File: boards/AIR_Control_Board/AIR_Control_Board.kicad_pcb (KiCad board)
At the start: 2 copper layers, 0 parts

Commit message: adding AIR folder
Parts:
- added C1: CP_1mF, footprints:C_Radial_D10_L13_P5_OEM, F.Cu at (231.1, 62.2)
- added C10: C_0.1uF, footprints:C_0805_OEM, F.Cu at (194.3, 67.3)
- added C2: C_0.1uF, footprints:C_0805_OEM, F.Cu at (191.8, 67.3)
- added C3: CP_1mF, footprints:C_Radial_D10_L13_P5_OEM, F.Cu at (217.2, 64.8)
- added C4: C_100pF, footprints:C_0805_OEM, F.Cu at (212.1, 52.1)
- added C5: C_22uF, footprints:C_1206_OEM, F.Cu at (210.6, 42.9)
- added C6: C_0.1uF, footprints:C_0805_OEM, F.Cu at (214.6, 38.1)
- added C7: C_30pF, footprints:C_0805_OEM, F.Cu at (207.0, 66.0)
- added C8: C_30pF, footprints:C_0805_OEM, F.Cu at (210.8, 67.3)
- added C9: C_47uF, footprints:C_0805_OEM, F.Cu at (221.0, 47.0)
- added D1: D_Schottky_SOD123, footprints:D_SOD-123W_OEM, F.Cu at (231.1, 52.1)
- added D10: LED_0805, footprints:LED_0805_OEM, F.Cu at (199.4, 48.3)
- added D11: D_Zener_18V, footprints:DO-214AA, F.Cu at (196.8, 39.4)
- added D2: D_Schottky_SOD123, footprints:D_SOD-123W_OEM, F.Cu at (232.4, 67.3)
- added D3: LED_0805, footprints:LED_0805_OEM, F.Cu at (198.8, 73.0)
- added D4: LED_0805, footprints:LED_0805_OEM, F.Cu at (210.2, 73.0)
- added D5: LED_0805, footprints:LED_0805_OEM, F.Cu at (222.9, 73.0)
- added D6: D_Schottky_SOD123, footprints:D_SOD-123W_OEM, F.Cu at (231.8, 40.0)
- added D7: LED_0805, footprints:LED_0805_OEM, F.Cu at (210.3, 38.4)
- added D8: LED_0805, footprints:LED_0805_OEM, F.Cu at (217.2, 52.1)
- added D9: LED_0805, footprints:LED_0805_OEM, F.Cu at (195.6, 48.3)
- added F1: F_500mA_16V, footprints:Fuse_1210, F.Cu at (203.2, 39.4)
- added IC1: ATMEGA16M1, footprints:TQFP-32_7x7mm_Pitch0.8mm, F.Cu at (204.5, 55.9)
- added J1: micromatch_female_RA_16, footprints:micromatch_female_ra_16, F.Cu at (189.2, 44.5)
- added J2: Ultrafit_2, footprints:Ultrafit_2, F.Cu at (243.8, 57.1)
- added J3: Ultrafit_2, footprints:Ultrafit_2, F.Cu at (243.8, 47.0)
- added J4: Ultrafit_2, footprints:Ultrafit_2, F.Cu at (243.8, 68.6)
- added J5: CONN_02X03, footprints:Pin_Header_Straight_2x03, F.Cu at (191.8, 77.5)
- added L1: L_4.7uH, footprints:4.7uH_Inductor_OEM, F.Cu at (222.2, 40.6)
- added Q1: NMOS_GSD_30V, TO_SOT_Packages_SMD:SOT-23, F.Cu at (233.7, 72.4)
- added Q2: NMOS_GSD_30V, TO_SOT_Packages_SMD:SOT-23, F.Cu at (200.0, 76.8)
- added Q3: NMOS_GSD_30V, TO_SOT_Packages_SMD:SOT-23, F.Cu at (211.5, 78.1)
- added Q4: NMOS_GSD_30V, TO_SOT_Packages_SMD:SOT-23, F.Cu at (224.2, 76.8)
- added Q5: NMOS_GSD_30V, TO_SOT_Packages_SMD:SOT-23, F.Cu at (231.8, 45.1)
- added R1: R_10k, footprints:R_0805_OEM, F.Cu at (200.0, 80.6)
- added R10: R_100k, footprints:R_0805_OEM, F.Cu at (225.4, 73.0)
- added R11: R_10k, footprints:R_0805_OEM, F.Cu at (233.7, 78.7)
- added R12: R_100, footprints:R_0805_OEM, F.Cu at (212.1, 49.5)
- added R13: R_1k, footprints:R_0805_OEM, F.Cu at (207.0, 39.6)
- added R14: R_10k, footprints:R_0805_OEM, F.Cu at (207.0, 43.2)
- added R15: R_10k, footprints:R_0805_OEM, F.Cu at (215.9, 47.0)
- added R16: R_55.1k, footprints:R_0805_OEM, F.Cu at (218.4, 47.0)
- added R17: R_200, footprints:R_0805_OEM, F.Cu at (198.1, 59.7)
- added R18: R_200, footprints:R_0805_OEM, F.Cu at (198.1, 62.2)
- added R19: R_10k, footprints:R_0805_OEM, F.Cu at (208.3, 49.5)
- added R2: R_10k, footprints:R_0805_OEM, F.Cu at (211.5, 81.9)
- added R20: R_0_Jumper, footprints:R_2512_OEM, F.Cu at (224.8, 49.5)
- added R21: R_200, footprints:R_0805_OEM, F.Cu at (221.0, 52.1)
- added R22: R_200, footprints:R_0805_OEM, F.Cu at (195.6, 44.5)
- added R23: R_200, footprints:R_0805_OEM, F.Cu at (199.4, 44.5)
- added R3: R_10k, footprints:R_0805_OEM, F.Cu at (220.3, 76.8)
- added R4: R_10k, footprints:R_0805_OEM, F.Cu at (231.8, 48.9)
- added R5: R_1k, footprints:R_0805_OEM, F.Cu at (196.2, 73.0)
- added R6: R_100k, footprints:R_0805_OEM, F.Cu at (196.2, 76.8)
- added R7: R_1k, footprints:R_0805_OEM, F.Cu at (207.6, 74.3)
- added R8: R_100k, footprints:R_0805_OEM, F.Cu at (207.6, 78.1)
- added R9: R_1k, footprints:R_0805_OEM, F.Cu at (220.3, 73.0)
- added U1: TPS561201, footprints:SOT-23-6_OEM, F.Cu at (214.6, 41.9)
- added U2: CAN_Transceiver, footprints:SOIC-8_3.9x4.9mm_Pitch1.27mm_OEM, F.Cu at (200.7, 67.3)
- added Y1: Crystal_SMD, footprints:Crystal_SMD_FA238, F.Cu at (210.8, 63.5)
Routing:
- net +12V: track 0.00 -> 13.0 mm
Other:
- net class Default: trace_width 0.1524 -> 0.254; via_dia 0.6 -> 0.6096; via_drill 0.4 -> 0.3048
- rule trace_min: 0.1524 -> 0.254
- rule via_min_drill: 0.3 -> 0.3048
- rule via_min_size: 0.4 -> 0.6096

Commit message: AIR Control 3D Model
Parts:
- moved J1 9.39 mm to (191.8, 53.5), turned to 180 degrees
- moved C1 5.70 mm to (231.4, 56.5)
- moved C3 5.51 mm to (222.7, 64.9)
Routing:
- net +12V: track 13.0 -> 6.59 mm
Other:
- board outline added: 70 x 70 mm

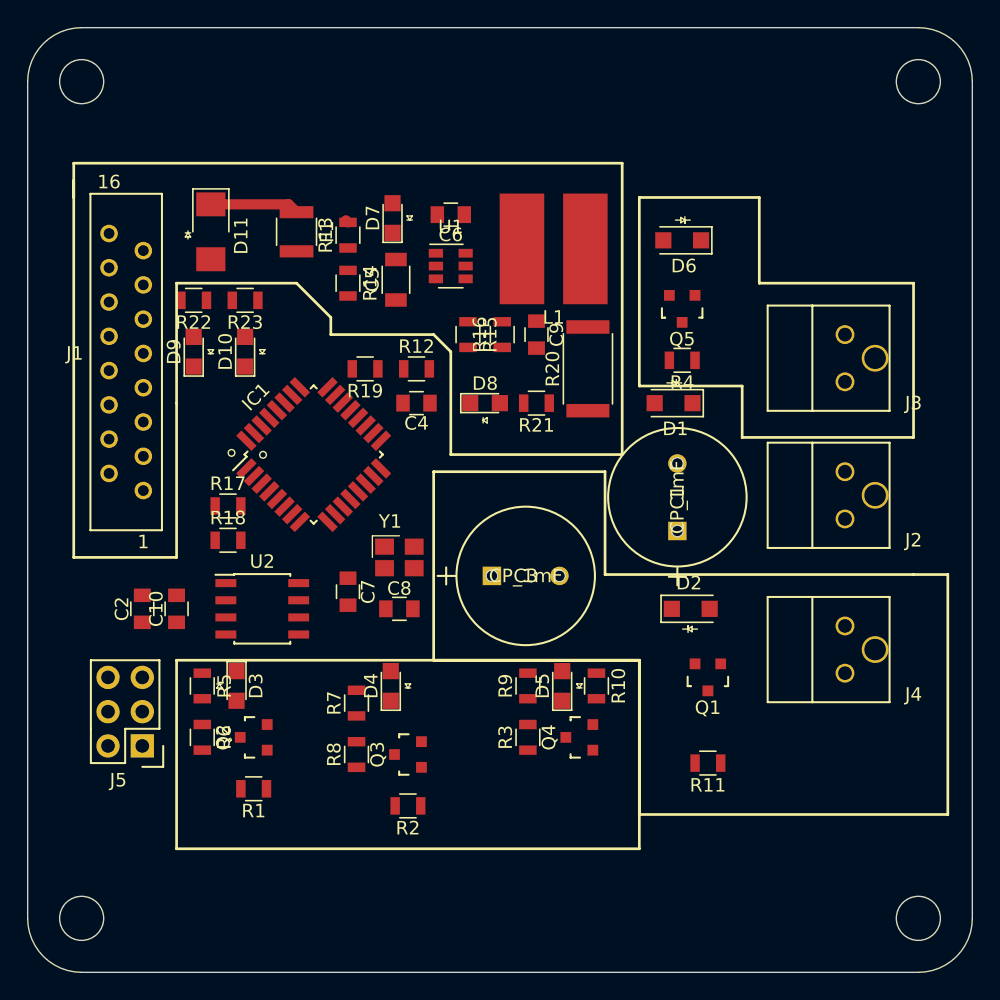
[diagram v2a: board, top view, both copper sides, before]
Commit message: Restored original air folder
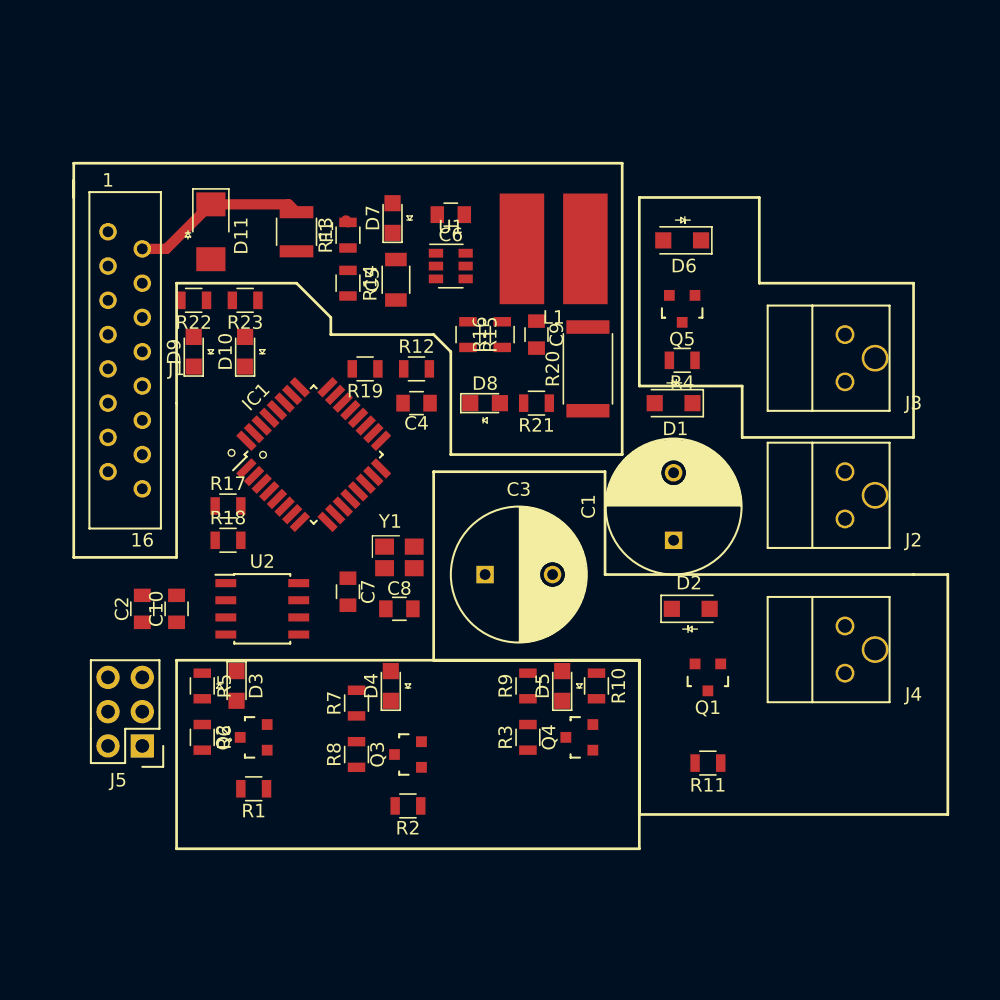
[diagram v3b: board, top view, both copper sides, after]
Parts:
- moved J1 9.39 mm to (189.2, 44.5), turned to 0 degrees
- moved C1 5.70 mm to (231.1, 62.2)
- moved C3 5.51 mm to (217.2, 64.8)
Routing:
- net +12V: track 6.59 -> 13.0 mm
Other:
- board outline removed

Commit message: Updated Layout
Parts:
- added D12: LED_0805, footprints:LED_0805_OEM, F.Cu at (205.9, 149.6)
- added D13: D_Schottky_SOD123, footprints:D_SOD-123W_OEM, F.Cu at (164.0, 155.4)
- added D14: D_Zener_18V, footprints:DO-214AA, F.Cu at (221.4, 119.3)
- added D15: LED_0805, footprints:LED_0805_OEM, F.Cu at (237.2, 118.5)
- added D16: LED_0805, footprints:LED_0805_OEM, F.Cu at (215.2, 144.0)
- added J6: CONN_02X03, footprints:Pin_Header_Straight_2x03, F.Cu at (179.9, 118.7)
- added Q6: NMOS_GSD_30V, footprints:SOT-23F, F.Cu at (189.1, 148.7)
- added Q7: NMOS_GSD_30V, footprints:SOT-23F, F.Cu at (210.7, 130.3)
- added R24: R_1k, footprints:R_0805_OEM, F.Cu at (247.1, 135.2)
- added R25: R_10k, footprints:R_0805_OEM, F.Cu at (229.2, 156.2)
- added R26: R_10k, footprints:R_0805_OEM, F.Cu at (239.4, 140.6)
- added R27: R_55.1k, footprints:R_0805_OEM, F.Cu at (223.9, 134.8)
- added R28: R_200, footprints:R_0805_OEM, F.Cu at (238.7, 145.9)
- added R29: R_200, footprints:R_0805_OEM, F.Cu at (244.3, 140.6)
- added R30: R_0_Jumper, footprints:R_2512_OEM, F.Cu at (221.1, 126.2)
- added R31: R_10k, footprints:R_0805_OEM, F.Cu at (232.8, 150.9)
- added R32: R_200, footprints:R_0805_OEM, F.Cu at (224.3, 156.2)
- C10: value C_0.1uF -> C_47uF
- C2: value C_0.1uF -> CP_1mF; footprint footprints:C_0805_OEM -> footprints:C_Radial_D10_L13_P5_OEM
- C3: value CP_1mF -> C_0.1uF; footprint footprints:C_Radial_D10_L13_P5_OEM -> footprints:C_0805_OEM
- C4: value C_100pF -> C_0.1uF
- C5: value C_22uF -> C_100pF; footprint footprints:C_1206_OEM -> footprints:C_0805_OEM
- C6: value C_0.1uF -> C_22uF; footprint footprints:C_0805_OEM -> footprints:C_1206_OEM
- C7: value C_30pF -> C_0.1uF
- C9: value C_47uF -> C_30pF
- D11: value D_Zener_18V -> LED_0805; footprint footprints:DO-214AA -> footprints:LED_0805_OEM
- D2, D6: value D_Schottky_SOD123 -> LED_0805; footprint footprints:D_SOD-123W_OEM -> footprints:LED_0805_OEM
- D7: value LED_0805 -> D_Schottky_SOD123; footprint footprints:LED_0805_OEM -> footprints:D_SOD-123W_OEM
- J1: value micromatch_female_RA_16 -> AIR-; footprint footprints:micromatch_female_ra_16 -> footprints:Ultrafit_4
- J3: value Ultrafit_2 -> To Interface Board; footprint footprints:Ultrafit_2 -> footprints:micromatch_female_ra_18
- J4: value Ultrafit_2 -> PrechargeRelay
- J5: value CONN_02X03 -> AIR+; footprint footprints:Pin_Header_Straight_2x03 -> footprints:Ultrafit_2
- Q1, Q2, Q3, Q4, Q5: footprint TO_SOT_Packages_SMD:SOT-23 -> footprints:SOT-23F
- R1, R4: value R_10k -> R_1k
- R11, R14, R15: value R_10k -> R_200
- R12: value R_100 -> R_10k
- R13: value R_1k -> R_10k
- R16: value R_55.1k -> R_10k
- R17, R18: value R_200 -> R_1k
- R19, R2: value R_10k -> R_100k
- R20: value R_0_Jumper -> R_100k; footprint footprints:R_2512_OEM -> footprints:R_0805_OEM
- R21, R22: value R_200 -> R_10k
- R23: value R_200 -> R_100
- R5: value R_1k -> R_200
- R6: value R_100k -> R_10k
- R8: value R_100k -> R_1k
- R9: value R_1k -> R_100k
- U1: value TPS561201 -> CAN_Transceiver; footprint footprints:SOT-23-6_OEM -> footprints:SOIC-8_3.9x4.9mm_Pitch1.27mm_OEM
- U2: value CAN_Transceiver -> TPS561201; footprint footprints:SOIC-8_3.9x4.9mm_Pitch1.27mm_OEM -> footprints:SOT-23-6_OEM
- moved D11 121.0 mm to (174.5, 158.3), turned to 0 degrees
- moved F1 116.9 mm to (188.5, 155.4), turned to 0 degrees
- moved R22 114.8 mm to (237.5, 151.3), turned to 0 degrees
- moved J2 114.2 mm to (177.2, 149.8)
- moved J3 111.2 mm to (157.8, 117.5)
- moved R23 110.7 mm to (243.6, 145.9), turned to 0 degrees
- moved R16 108.0 mm to (215.7, 154.9), turned to 0 degrees
- moved Q5 106.9 mm to (186.2, 141.7), turned to 0 degrees
- moved R13 104.3 mm to (234.7, 140.2), turned to 0 degrees
- moved J1 104.0 mm to (162.2, 144.9)
- moved R14 103.7 mm to (224.1, 145.5), turned to 0 degrees
- moved R21 101.5 mm to (242.3, 151.3), turned to 0 degrees
- moved D9 101.3 mm to (198.3, 149.6), turned to 0 degrees
- moved R19 100.6 mm to (218.8, 149.6), turned to 0 degrees
- moved U1 100.2 mm to (174.5, 133.7)
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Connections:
- C10 pad 1: VCC -> Net-(C10-Pad1)
- C2 pad 1: VCC -> /ShutdownIn
- C2 pad 2: GND -> Net-(C2-Pad2)
- C3 pad 1: /ShutdownIn -> VCC
- C4 pad 1: Net-(C4-Pad1) -> VCC
- C5 pad 1: /12V_Fused -> Net-(C5-Pad1)
- C6 pad 1: Net-(C6-Pad1) -> /12V_Fused
- C6 pad 2: Net-(C6-Pad2) -> GND
- C7 pad 2: GND -> Net-(C7-Pad2)
- D11 pad 1: +12V -> GND
- D11 pad 2: GND -> Net-(D11-Pad2)
- D2 pad 1: /ShutdownIn -> GND
- D6 pad 1: /ShutdownIn -> GND
- D7 pad 1: GND -> /ShutdownIn
- IC1 pad 10: Net-(C8-Pad1) -> Net-(C9-Pad1)
- IC1 pad 11: Net-(C7-Pad1) -> Net-(C8-Pad1)
- IC1 pad 13: Net-(IC1-Pad13) -> /SenseBMS
- IC1 pad 14: Net-(IC1-Pad14) -> /SenseIMD
- IC1 pad 15: Net-(IC1-Pad15) -> /SenseMainTSConn
- IC1 pad 16: Net-(IC1-Pad16) -> /SenseConnToHVD
- IC1 pad 17: Net-(IC1-Pad17) -> /AIR+LSD
- IC1 pad 18: Net-(IC1-Pad18) -> /PrechargeCTL
- IC1 pad 19: Net-(C4-Pad1) -> Net-(C5-Pad1)
- IC1 pad 22: /AIR+LSD -> /AIR-_Weld_Detect
- IC1 pad 23: /PrechargeCTL -> Net-(IC1-Pad23)
- IC1 pad 24: /SenseBMS -> Net-(IC1-Pad24)
- IC1 pad 26: /SenseIMD -> Net-(IC1-Pad26)
- IC1 pad 27: /SenseMainTSConn -> Net-(IC1-Pad27)
- IC1 pad 28: /IMDStatus -> Net-(IC1-Pad28)
- IC1 pad 29: /BMSStatus -> /IMDStatus
- IC1 pad 3: /ProgrammingLED2 -> Net-(IC1-Pad3)
- IC1 pad 30: /ProgrammingLED1 -> /BMSStatus
- IC1 pad 6: Net-(IC1-Pad6) -> /TXCAN
- IC1 pad 7: Net-(IC1-Pad7) -> /RXCAN
- IC1 pad 8: Net-(IC1-Pad8) -> /ProgrammingLED1
- IC1 pad 9: Net-(IC1-Pad9) -> /ProgrammingLED2
- J1 pad 1: GND -> /12V_Fused
- J1 pad 2: +12V -> /Aux_Contact-
- J1 pad 3: VCC -> /ShutdownIn
- J1 pad 4: /MOSI -> GND
- J2 pad 2: GND -> Net-(J2-Pad2)
- J3 pad 1: Net-(D2-Pad2) -> GND
- J3 pad 2: /ShutdownIn -> +12V
- J4 pad 1: /ShutdownIn -> Net-(D7-Pad2)
- J4 pad 2: Net-(D6-Pad2) -> /ShutdownIn
- J5 pad 1: /MISO -> /ShutdownIn
- J5 pad 2: VCC -> Net-(C2-Pad2)
- L1 pad 1: Net-(C6-Pad2) -> Net-(C7-Pad2)
- L1 pad 2: Net-(C9-Pad1) -> Net-(C10-Pad1)
- Q1 pad 1: /PrechargeCTL -> /Aux_Contact-
- Q1 pad 3: Net-(D2-Pad2) -> /AIR-_Weld_Detect
- Q2 pad 1: /ShutdownSenseBMS -> /PrechargeCTL
- Q2 pad 3: /SenseBMS -> Net-(D7-Pad2)
- Q3 pad 1: /ShutdownSenseIMD -> /ShutdownSenseConnToHVD
- Q3 pad 3: /SenseIMD -> /SenseConnToHVD
- Q5 pad 3: Net-(D6-Pad2) -> Net-(C2-Pad2)
- R1 pad 1: VCC -> Net-(D2-Pad2)
- R1 pad 2: /SenseBMS -> /Aux_Contact-
- R11 pad 1: /AIR+LSD -> /ProgrammingLED1
- R11 pad 2: GND -> Net-(D8-Pad2)
- R12 pad 2: Net-(C4-Pad1) -> /SenseConnToHVD
- R13 pad 1: /12V_Fused -> VCC
- R13 pad 2: Net-(D7-Pad2) -> /SenseMainTSConn
- R14 pad 1: /12V_Fused -> /ProgrammingLED2
- R14 pad 2: Net-(R14-Pad2) -> Net-(D9-Pad2)
- R15 pad 1: Net-(R15-Pad1) -> /AIR+LSD
- R15 pad 2: GND -> Net-(D10-Pad2)
- R16 pad 1: Net-(R15-Pad1) -> /AIR+LSD
- R16 pad 2: Net-(C9-Pad1) -> GND
- R17 pad 1: /LED1 -> Net-(D11-Pad2)
- R17 pad 2: Net-(IC1-Pad8) -> /ShutdownSenseBMS
- R18 pad 1: /LED2 -> Net-(D12-Pad2)
- R18 pad 2: Net-(IC1-Pad9) -> /ShutdownSenseIMD
- R19 pad 1: VCC -> /ShutdownSenseBMS
- R19 pad 2: /RESET -> GND
- R2 pad 1: VCC -> /Aux_Contact-
- R2 pad 2: /SenseIMD -> GND
- R20 pad 1: VCC -> /ShutdownSenseIMD
- R20 pad 2: Net-(C9-Pad1) -> GND
- R21 pad 2: Net-(D8-Pad2) -> /SenseBMS
- R22 pad 1: /ProgrammingLED1 -> VCC
- R22 pad 2: Net-(D9-Pad2) -> /SenseIMD
- R23 pad 1: /ProgrammingLED2 -> VCC
- R23 pad 2: Net-(D10-Pad2) -> Net-(C5-Pad1)
- R3 pad 2: /SenseMainTSConn -> /AIR-_Weld_Detect
- R4 pad 1: /PrechargeCTL -> /ShutdownIn
- R4 pad 2: GND -> Net-(D3-Pad2)
- R5 pad 1: Net-(D3-Pad2) -> /PrechargeCTL
- R5 pad 2: /ShutdownSenseBMS -> Net-(D4-Pad2)
- R6 pad 1: /ShutdownSenseBMS -> /PrechargeCTL
- R7 pad 1: Net-(D4-Pad2) -> Net-(D5-Pad2)
- R7 pad 2: /ShutdownSenseIMD -> /ShutdownSenseConnToHVD
- R8 pad 1: /ShutdownSenseIMD -> Net-(D6-Pad2)
- R8 pad 2: GND -> /ShutdownSenseMainTSConn
- R9 pad 1: Net-(D5-Pad2) -> /ShutdownSenseConnToHVD
- R9 pad 2: /ShutdownSenseMainTSConn -> GND
- U1 pad 1: GND -> /TXCAN
- U1 pad 2: Net-(C6-Pad2) -> GND
- U1 pad 3: /12V_Fused -> VCC
- U1 pad 4: Net-(R15-Pad1) -> /RXCAN
- U1 pad 5: Net-(R14-Pad2) -> Net-(U1-Pad5)
- U1 pad 6: Net-(C6-Pad1) -> /CANL
- U2 pad 1: Net-(IC1-Pad6) -> GND
- U2 pad 2: GND -> Net-(C7-Pad2)
- U2 pad 3: VCC -> /12V_Fused
- U2 pad 4: Net-(IC1-Pad7) -> Net-(R26-Pad1)
- U2 pad 6: /CANL -> Net-(C7-Pad1)
- Y1 pad 1: Net-(C7-Pad1) -> Net-(C8-Pad1)
- Y1 pad 3: Net-(C8-Pad1) -> Net-(C9-Pad1)
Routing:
- net +12V: track 13.0 -> 0.00 mm
